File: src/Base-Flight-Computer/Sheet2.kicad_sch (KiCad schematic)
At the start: 11 parts, among them P1 1984659, Q5 2N7002W-7-F, Q6 2N7002W-7-F, U4 SST25VF040B-50-4I-S2AE-T

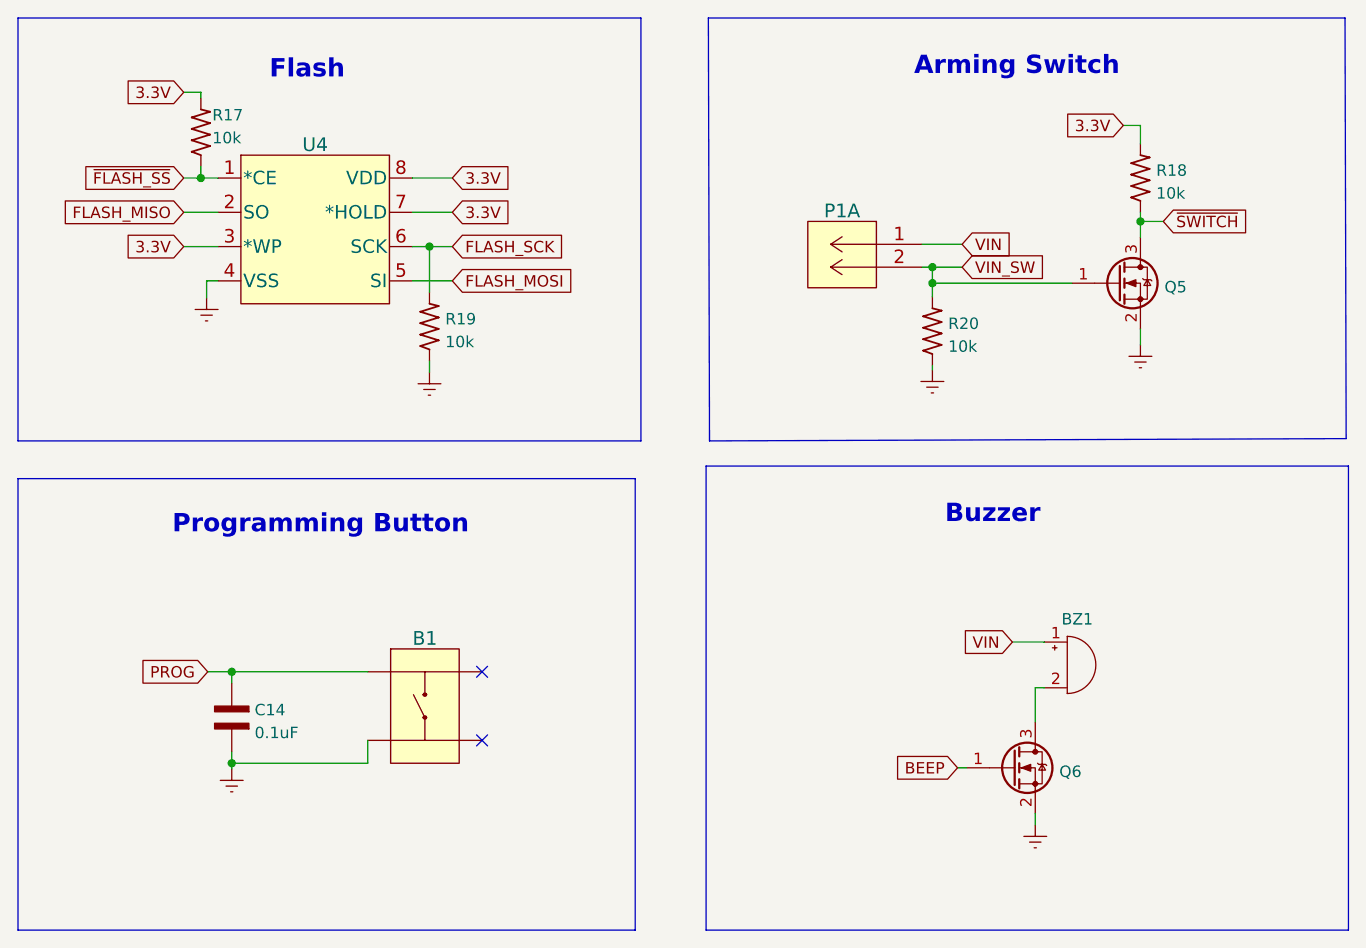
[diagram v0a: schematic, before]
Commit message: removed programming button
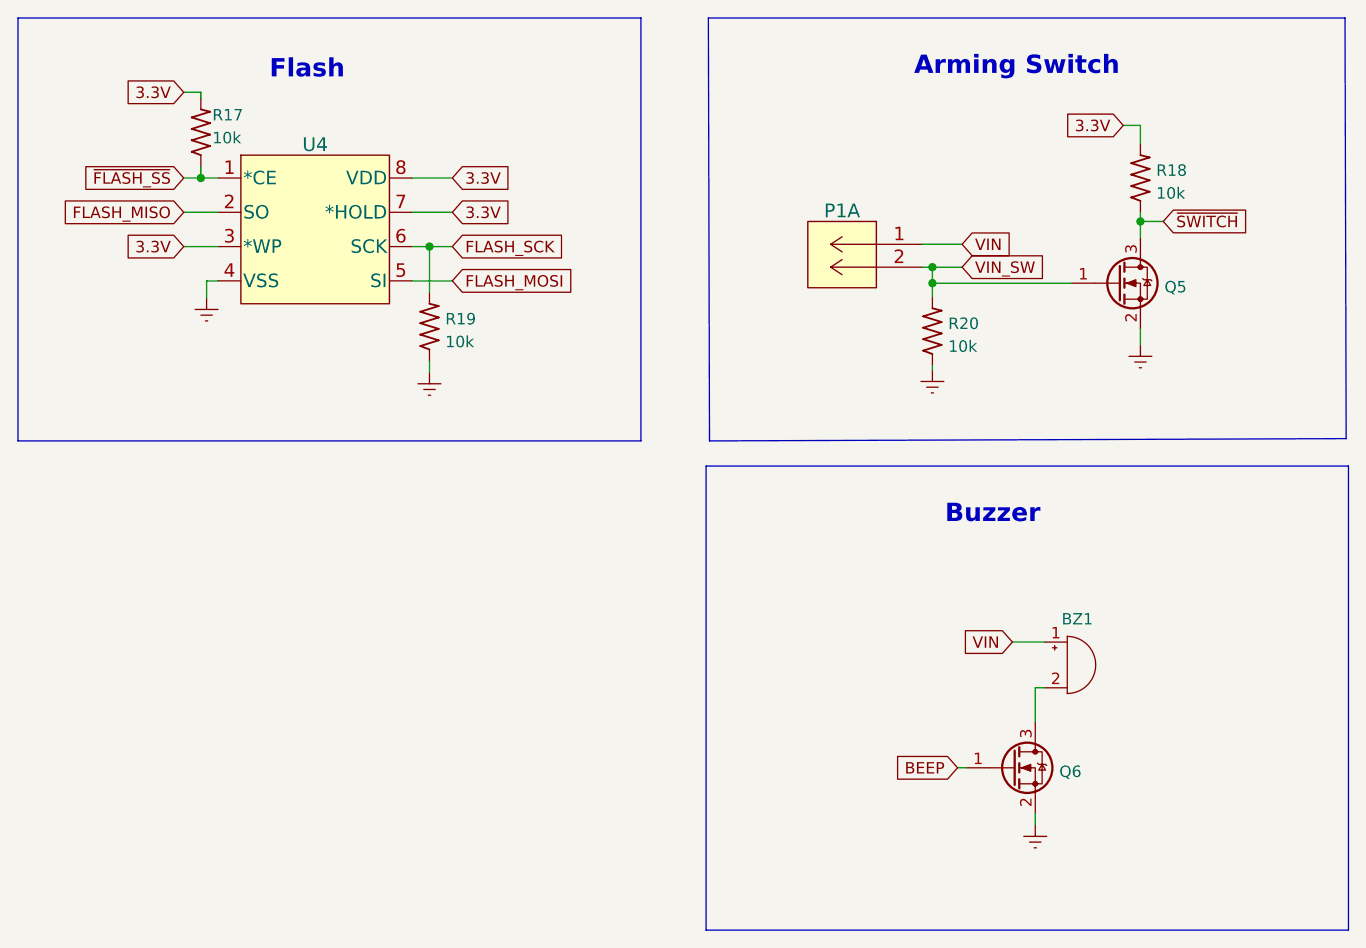
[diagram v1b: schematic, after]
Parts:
- removed B1: PTS647SM38SMTR2LFS, Flight-Computer-Lite:PTS647SM38SMTR2LFS, symbol Flight-Computer:PTS647SM38SMTR2LFS
- removed C14: 0.1uF, Flight-Computer-Lite:CAP_0603, symbol Flight-Computer:CAP_0603
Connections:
- no-connect marks 2 -> 0
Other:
- note removed: "Programming Button"

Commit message: updated schematic links to new library files
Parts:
- BZ1: footprint Flight-Computer-Lite:AT-1438-TWT-R -> Flight-Computer:AT-1438-TWT-R
- P1: footprint Flight-Computer-Lite:1984659 -> Flight-Computer:1984659
- Q5, Q6: footprint Flight-Computer-Lite:2N7002W-7-F -> Flight-Computer-Lite:QS5U17TR
- U4: footprint Flight-Computer-Lite:SST25VF040B-50-4I-S2AE-T -> SOIC8_S2A_SST_MCH
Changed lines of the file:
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@@
       (effects (font (size 1.27 1.27)) (justify left) hide)
     )
-    (property "Footprint" "Flight-Computer-Lite:2N7002W-7-F" (at 186.817 77.851 0)
+    (property "Footprint" "Flight-Computer-Lite:QS5U17TR" (at 186.817 77.851 0)
       (effects (font (size 1.27 1.27) italic) (justify left) hide)
     )
@@
       (effects (font (size 1.27 1.27)) (justify left) hide)
     )
-    (property "Footprint" "Flight-Computer-Lite:AT-1438-TWT-R" (at 178.689 101.854 90)
+    (property "Footprint" "Flight-Computer:AT-1438-TWT-R" (at 178.689 101.854 90)
       (effects (font (size 1.27 1.27)) hide)
     )
@@
       (effects (font (size 1.524 1.524)) hide)
     )
-    (property "Footprint" "Flight-Computer-Lite:1984659" (at 159.385 88.138 0)
+    (property "Footprint" "Flight-Computer:1984659" (at 159.385 88.138 0)
       (effects (font (size 1.524 1.524)) hide)
     )
@@
       (effects (font (size 1.27 1.27)) (justify left) hide)
     )
-    (property "Footprint" "Flight-Computer-Lite:2N7002W-7-F" (at 175.133 131.699 0)
+    (property "Footprint" "Flight-Computer-Lite:QS5U17TR" (at 175.133 131.699 0)
       (effects (font (size 1.27 1.27) italic) (justify left) hide)
     )
@@
       (effects (font (size 1.524 1.524)) hide)
     )
-    (property "Footprint" "Flight-Computer-Lite:SST25VF040B-50-4I-S2AE-T" (at 96.393 70.612 0)
-      (effects (font (size 1.524 1.524)) hide)
-    )
+    (property "Footprint" "SOIC8_S2A_SST_MCH" (at 96.393 70.612 0)
+      (effects (font (size 1.524 1.524)) hide)
+    )

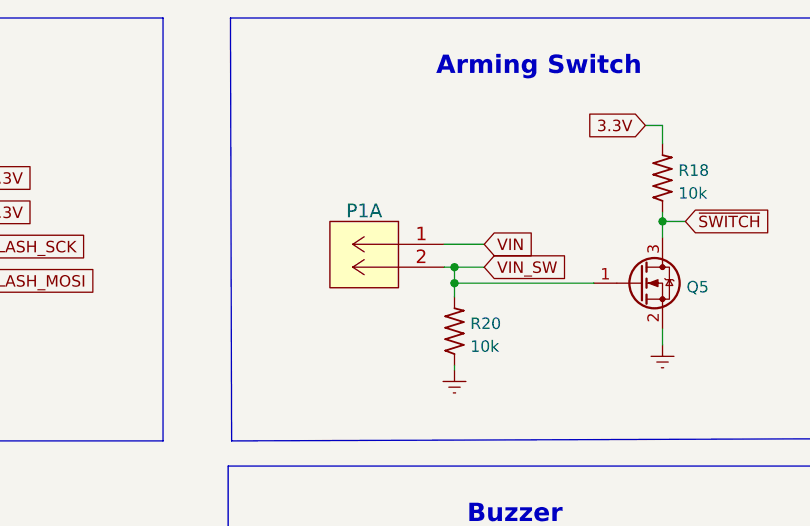
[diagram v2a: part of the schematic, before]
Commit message: added new screw terminals to schematic
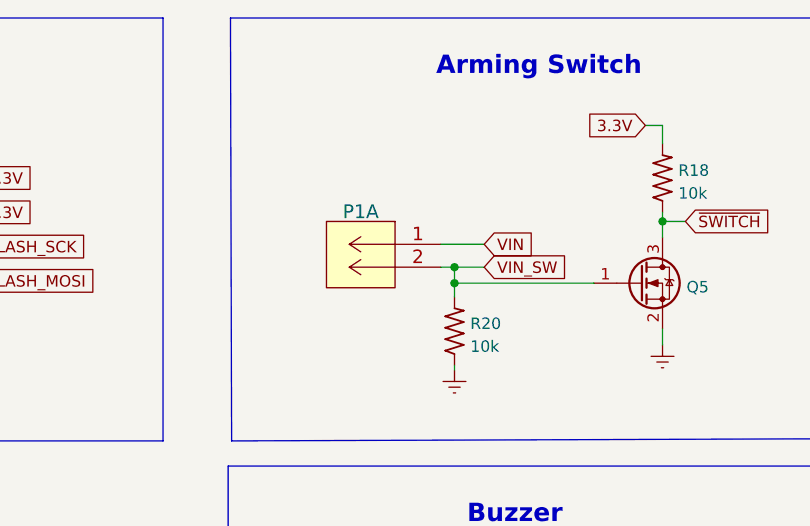
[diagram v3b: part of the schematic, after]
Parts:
- removed P1: 1984659, Flight-Computer:1984659, symbol Flight-Computer:1984659
- added P1: 1984659, Base-Flight-Computer:1984659, symbol Base-Flight-Computer:284391-6
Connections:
- net VIN: now also P1.1 (5)
- net VIN_SW: now also P1.2 (6)
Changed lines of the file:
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@@
-    (stroke (width 0) (type default))
-  )
-  (wire (pts (xy 163.195 57.658) (xy 167.64 57.658))
     (stroke (width 0) (type default))
   )
@@
     (stroke (width 0) (type default))
   )
-  (wire (pts (xy 163.195 60.198) (xy 164.338 60.198))
-    (stroke (width 0) (type default))
-  )
   (wire (pts (xy 185.547 44.45) (xy 187.452 44.45))
     (stroke (width 0) (type default))
@@
     (stroke (width 0) (type default))
   )
+  (wire (pts (xy 162.814 57.658) (xy 167.64 57.658))
+    (stroke (width 0) (type default))
+  )
   (wire (pts (xy 187.452 54.102) (xy 187.452 55.118))
     (stroke (width 0) (type default))
   )
   (polyline (pts (xy 131.953 79.502) (xy 62.738 79.502))
+    (stroke (width 0) (type default))
+  )
+  (wire (pts (xy 162.814 60.198) (xy 164.338 60.198))
     (stroke (width 0) (type default))
   )
@@
     )
   )
-  (symbol (lib_id "Flight-Computer:1984659") (at 163.195 57.658 0) (mirror y) (unit 1)
-    (in_bom yes) (on_board yes) (dnp no) (fields_autoplaced)
-    (property "Reference" "P1" (at 154.305 53.9511 0)
+  (symbol (lib_id "Flight-Computer-Lite:2N7002W-7-F") (at 173.228 115.824 0) (unit 1)
+    (in_bom yes) (on_board yes) (dnp no) (fields_autoplaced)
+    (property "Reference" "Q6" (at 178.435 116.2578 0)
+      (effects (font (size 1.27 1.27)) (justify left))
+    )
+    (property "Value" "2N7002W-7-F" (at 176.403 128.524 0)
+      (effects (font (size 1.27 1.27)) (justify left) hide)
+    )
+    (property "Footprint" "Flight-Computer-Lite:QS5U17TR" (at 175.133 131.699 0)
+      (effects (font (size 1.27 1.27) italic) (justify left) hide)
+    )
+    (property "Datasheet" "https://www.onsemi.com/pub/Collateral/NDS7002A-D.PDF" (at 171.958 134.874 0)
+      (effects (font (size 1.27 1.27)) (justify left) hide)
+    )
+    (pin "1")
+    (pin "2")
+    (pin "3")
+    (instances
+      (project "Base-Flight-Computer"
+        (path "/13f33ffc-3ab1-449a-9be0-c2c7f72f3b48/f45e6aa6-d67e-481b-8dba-bf06dba939fd"
+          (reference "Q6") (unit 1)
+        )
+      )
+    )
+  )
+  (symbol (lib_id "Base-Flight-Computer:284391-6") (at 162.814 57.658 0) (mirror y) (unit 1)
+    (in_bom yes) (on_board yes) (dnp no) (fields_autoplaced)
+    (property "Reference" "P1" (at 153.924 54.0399 0)
       (effects (font (size 1.524 1.524)))
     )
-    (property "Value" "1984659" (at 158.115 85.598 0)
+    (property "Value" "1984659" (at 157.734 85.598 0)
       (effects (font (size 1.524 1.524)) hide)
     )
-    (property "Footprint" "Flight-Computer:1984659" (at 159.385 88.138 0)
+    (property "Footprint" "Base-Flight-Computer:1984659" (at 159.004 88.138 0)
       (effects (font (size 1.524 1.524)) hide)
     )
-    (property "Datasheet" "" (at 163.195 57.658 0)
+    (property "Datasheet" "" (at 162.814 57.658 0)
       (effects (font (size 1.524 1.524)) hide)
     )
@@
         )
       )
-    )
-  )
-  (symbol (lib_id "Flight-Computer-Lite:2N7002W-7-F") (at 173.228 115.824 0) (unit 1)
-    (in_bom yes) (on_board yes) (dnp no) (fields_autoplaced)
-    (property "Reference" "Q6" (at 178.435 116.2578 0)
-      (effects (font (size 1.27 1.27)) (justify left))
-    )
-    (property "Value" "2N7002W-7-F" (at 176.403 128.524 0)
-      (effects (font (size 1.27 1.27)) (justify left) hide)
-    )
-    (property "Footprint" "Flight-Computer-Lite:QS5U17TR" (at 175.133 131.699 0)
-      (effects (font (size 1.27 1.27) italic) (justify left) hide)
-    )
-    (property "Datasheet" "https://www.onsemi.com/pub/Collateral/NDS7002A-D.PDF" (at 171.958 134.874 0)
-      (effects (font (size 1.27 1.27)) (justify left) hide)
-    )
-    (pin "1")
-    (pin "2")
-    (pin "3")
-    (instances
-      (project "Base-Flight-Computer"
-        (path "/13f33ffc-3ab1-449a-9be0-c2c7f72f3b48/f45e6aa6-d67e-481b-8dba-bf06dba939fd"
-          (reference "Q6") (unit 1)
-        )
-      )

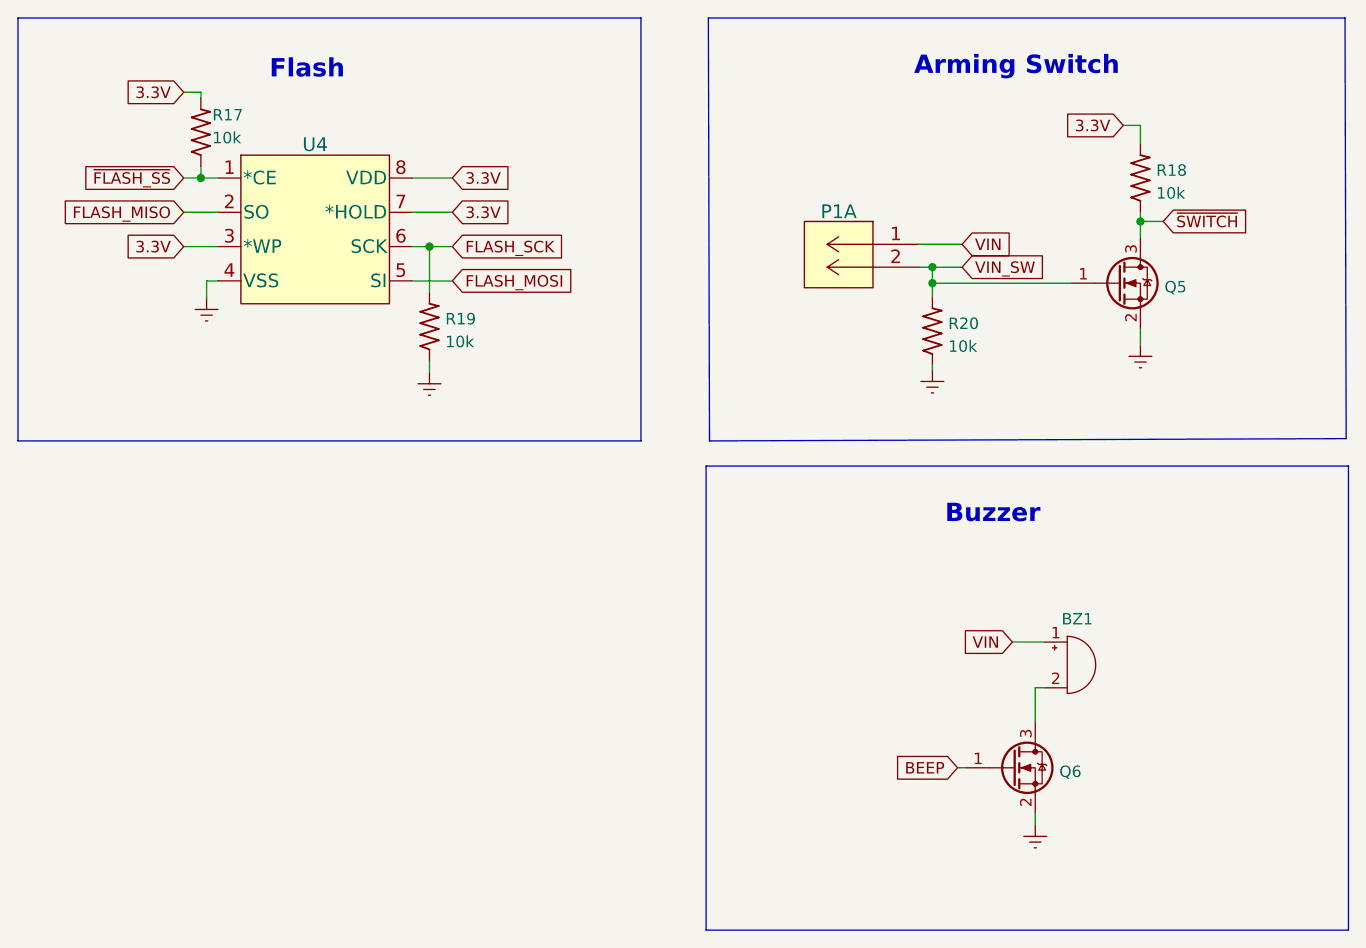
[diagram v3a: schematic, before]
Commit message: updated schematic with 0402 resistors and capacitors
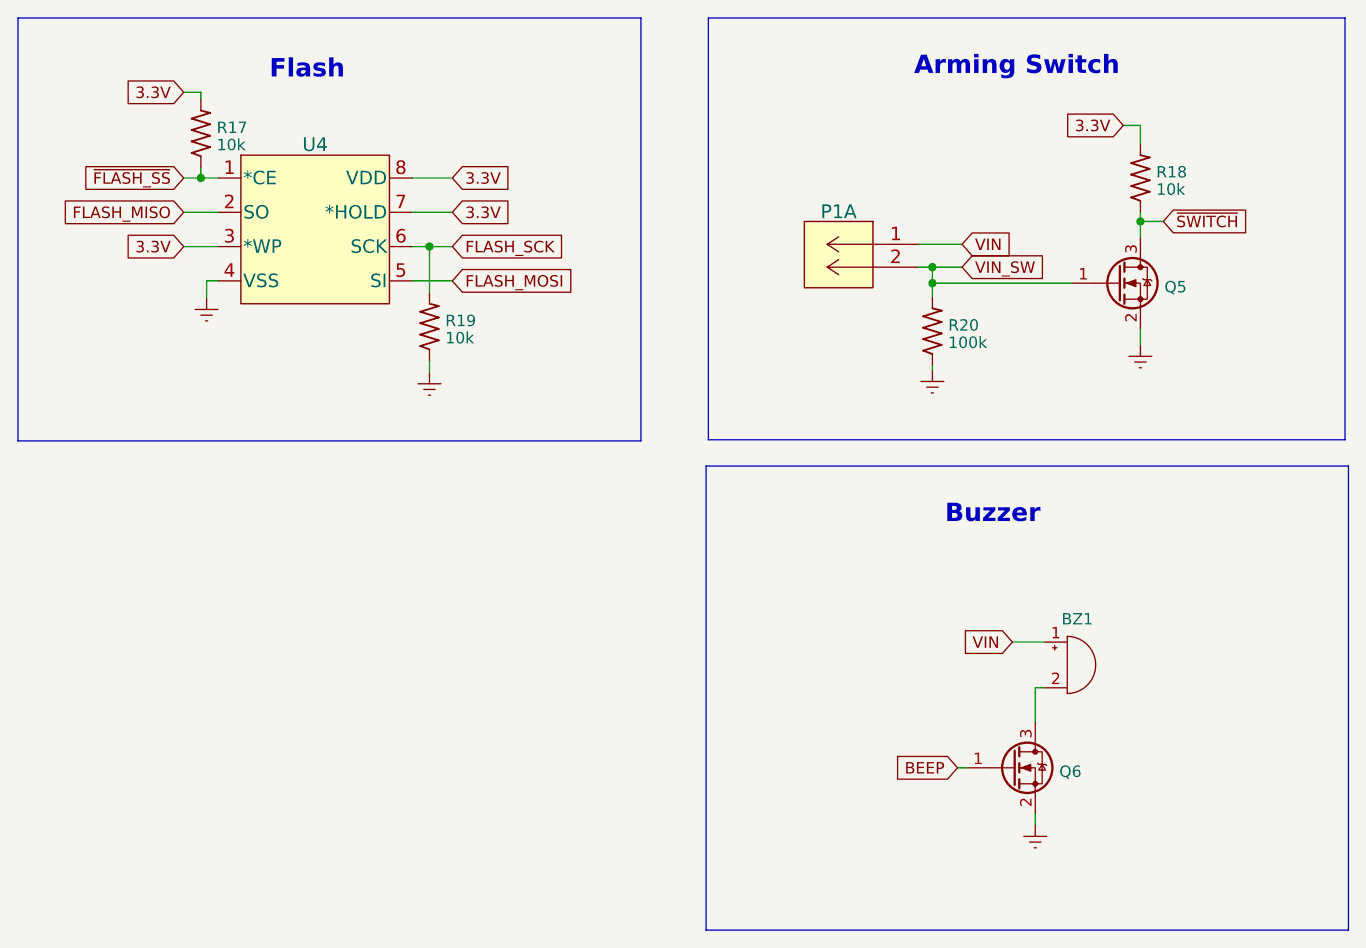
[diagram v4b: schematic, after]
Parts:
- removed R17, R18, R19, R20: 10k, Flight-Computer-Lite:RES_0603, symbol Flight-Computer:RES_0603
- added R17, R18, R19: 10k, Base-Flight-Computer:RES_0402, symbol Base-Flight-Computer:RES_0402
- added R20: 100k, Base-Flight-Computer:RES_0402, symbol Base-Flight-Computer:RES_0402
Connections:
- net 3.3V: now also R17.2, R18.2
- net Earth: now also R19.1, R20.1
- net FLASH_SCK: now also R19.2
- net VIN_SW: now also R20.2
- net ~{FLASH_SS}: now also R17.1
- net ~{SWITCH}: now also R18.1
